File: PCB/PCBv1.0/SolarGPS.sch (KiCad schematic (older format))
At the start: 53 parts, among them J1 Conn_01x10_Female, J2 Solar1+, J3 GND, J4 Conn_02x05_Odd_Even, J5 Solar2+, J6 GND, J7 Screw_Terminal_01x01, U2 MAX-M10Q, U3 MAX40200AUK, U4 STM32WB5MMGH6TR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

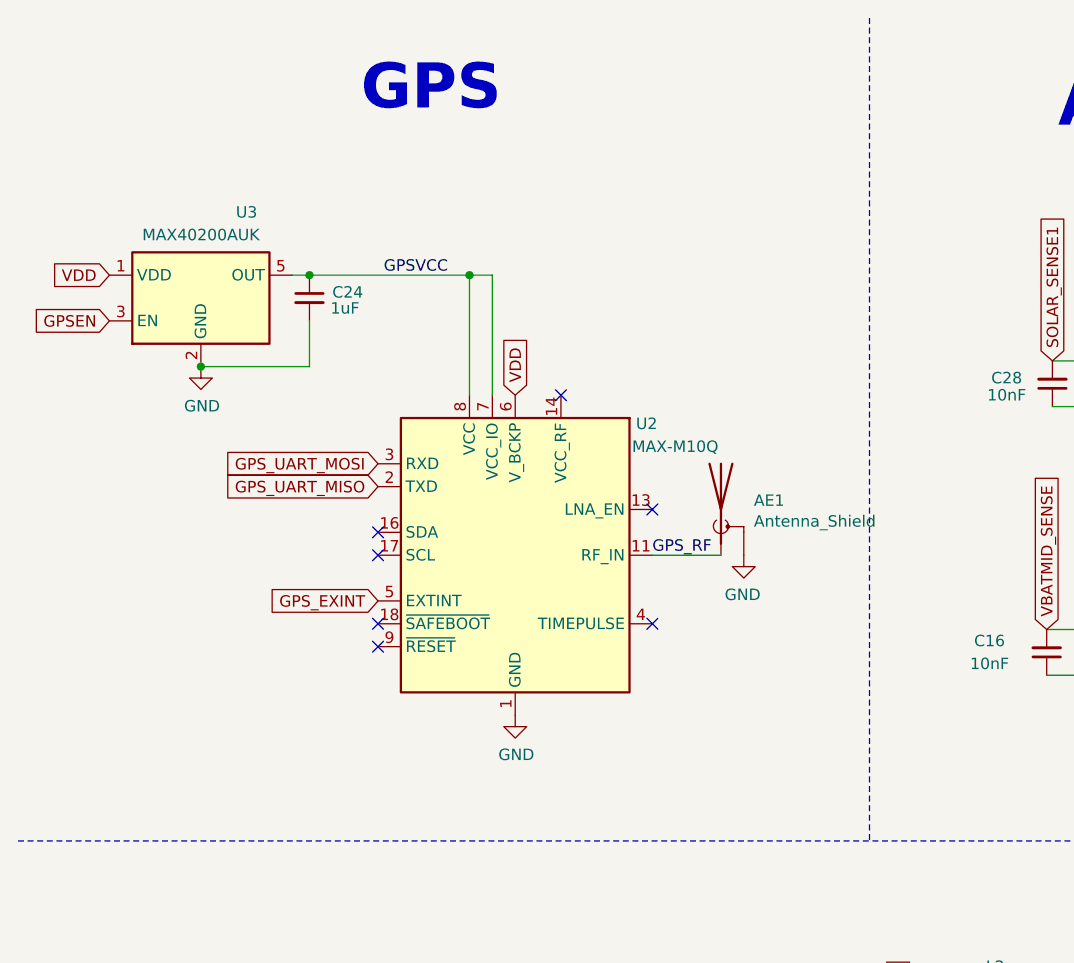
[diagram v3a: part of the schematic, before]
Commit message: Replace Antenna
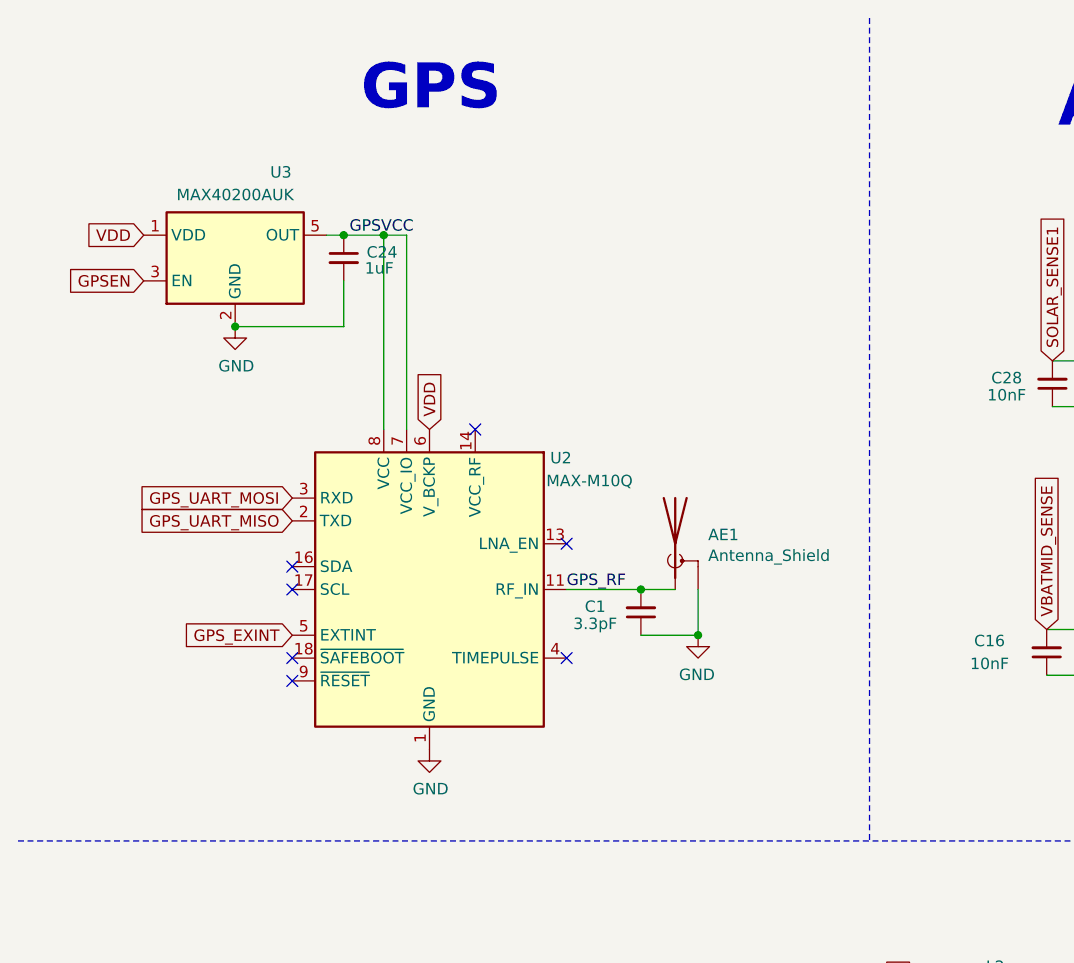
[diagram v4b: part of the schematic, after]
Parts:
- added C1: 3.3pF, Capacitor_SMD:C_0402_1005Metric, symbol Device:C_Small
- AE1: footprint Margo_Lib:LINX_CONSMA002-SMD -> RF_Antenna:Pulse_W3011; Part (none) -> W3011A
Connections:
- net GND: now also C1.1
- net GPS_RF: now also C1.2
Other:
- moved on the sheet: AE1, C24, U2, U3
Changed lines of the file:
@@
 Text GLabel 5000 1975 1    50   Input ~ 0
 SOLAR_SENSE1
-Connection ~ 1750 1600
+Connection ~ 1900 1425
 $Comp
 L Device:C_Small C24
 U 1 1 5FA4FE7E
-P 1750 1700
-F 0 "C24" H 1850 1725 50  0000 L CNN
-F 1 "1uF" H 1842 1655 50  0000 L CNN
-F 2 "Capacitor_SMD:C_0603_1608Metric" H 1750 1700 50  0001 C CNN
-F 3 "~" H 1750 1700 50  0001 C CNN
-	1    1750 1700
-	1    0    0    -1
-$EndComp
-Text GLabel 2050 3025 0    50   Input ~ 0
+P 1900 1525
+F 0 "C24" H 2000 1550 50  0000 L CNN
+F 1 "1uF" H 1992 1480 50  0000 L CNN
+F 2 "Capacitor_SMD:C_0603_1608Metric" H 1900 1525 50  0001 C CNN
+F 3 "~" H 1900 1525 50  0001 C CNN
+	1    1900 1525
+	1    0    0    -1
+$EndComp
+Text GLabel 1675 3175 0    50   Input ~ 0
 GPS_EXINT
 $Comp
 L power:GND #PWR015
 U 1 1 5FA4E6CF
-P 2650 3525
-F 0 "#PWR015" H 2650 3275 50  0001 C CNN
-F 1 "GND" H 2655 3352 50  0000 C CNN
-F 2 "" H 2650 3525 50  0001 C CNN
-F 3 "" H 2650 3525 50  0001 C CNN
-	1    2650 3525
+P 2275 3675
+F 0 "#PWR015" H 2275 3425 50  0001 C CNN
+F 1 "GND" H 2280 3502 50  0000 C CNN
+F 2 "" H 2275 3675 50  0001 C CNN
+F 3 "" H 2275 3675 50  0001 C CNN
+	1    2275 3675
 	1    0    0    -1
 $EndComp
@@
 L RF_GPS:MAX-M8Q U2
 U 1 1 6017075D
-P 2650 2825
-F 0 "U2" H 3225 3400 50  0000 C CNN
-F 1 "MAX-M10Q" H 3350 3300 50  0000 C CNN
-F 2 "RF_GPS:ublox_MAX" H 3050 2175 50  0001 C CNN
-F 3 "https://www.u-blox.com/sites/default/files/MAX-M8-FW3_DataSheet_%28UBX-15031506%29.pdf" H 2650 2825 50  0001 C CNN
-	1    2650 2825
-	1    0    0    -1
-$EndComp
-NoConn ~ 2050 2725
-NoConn ~ 2050 2825
-NoConn ~ 2050 3125
-NoConn ~ 2050 3225
-NoConn ~ 3250 3125
-NoConn ~ 3250 2625
-NoConn ~ 2850 2125
-Text GLabel 2050 2425 0    50   Input ~ 0
+P 2275 2975
+F 0 "U2" H 2850 3550 50  0000 C CNN
+F 1 "MAX-M10Q" H 2975 3450 50  0000 C CNN
+F 2 "RF_GPS:ublox_MAX" H 2675 2325 50  0001 C CNN
+F 3 "https://www.u-blox.com/sites/default/files/MAX-M8-FW3_DataSheet_%28UBX-15031506%29.pdf" H 2275 2975 50  0001 C CNN
+	1    2275 2975
+	1    0    0    -1
+$EndComp
+NoConn ~ 1675 2875
+NoConn ~ 1675 2975
+NoConn ~ 1675 3275
+NoConn ~ 1675 3375
+NoConn ~ 2875 3275
+NoConn ~ 2875 2775
+NoConn ~ 2475 2275
+Text GLabel 1675 2575 0    50   Input ~ 0
 GPS_UART_MOSI
-Text GLabel 2050 2525 0    50   Input ~ 0
+Text GLabel 1675 2675 0    50   Input ~ 0
 GPS_UART_MISO
 Wire Wire Line
@@
 Wire Wire Line
 	4425 7550 4425 7050
-Text GLabel 875  1600 0    50   Input ~ 0
+Text GLabel 1025 1425 0    50   Input ~ 0
 VDD
 Wire Wire Line
-	1675 1600 1750 1600
+	1825 1425 1900 1425
 $Comp
 L Connector:Conn_01x10_Female J1
@@
 SPI_MOSI
 Wire Wire Line
-	3250 2825 3550 2825
+	2875 2975 3200 2975
 Wire Wire Line
 	5675 3150 5950 3150
@@
 L Analog_Switch:MAX40200AUK U3
 U 1 1 61BA8BAE
-P 1275 1700
-F 0 "U3" H 1475 2075 50  0000 C CNN
-F 1 "MAX40200AUK" H 1275 1976 50  0000 C CNN
-F 2 "Package_TO_SOT_SMD:SOT-23-5" H 1275 2200 50  0001 C CNN
-F 3 "https://datasheets.maximintegrated.com/en/ds/MAX40200.pdf" H 1275 2200 50  0001 C CNN
-	1    1275 1700
-	1    0    0    -1
-$EndComp
-Text GLabel 875  1800 0    50   Input ~ 0
+P 1425 1525
+F 0 "U3" H 1625 1900 50  0000 C CNN
+F 1 "MAX40200AUK" H 1425 1801 50  0000 C CNN
+F 2 "Package_TO_SOT_SMD:SOT-23-5" H 1425 2025 50  0001 C CNN
+F 3 "https://datasheets.maximintegrated.com/en/ds/MAX40200.pdf" H 1425 2025 50  0001 C CNN
+	1    1425 1525
+	1    0    0    -1
+$EndComp
+Text GLabel 1025 1625 0    50   Input ~ 0
 GPSEN
 $Comp
 L power:GND #PWR06
 U 1 1 61BB7ABB
-P 1275 2000
-F 0 "#PWR06" H 1275 1750 50  0001 C CNN
-F 1 "GND" H 1280 1827 50  0000 C CNN
-F 2 "" H 1275 2000 50  0001 C CNN
-F 3 "" H 1275 2000 50  0001 C CNN
-	1    1275 2000
+P 1425 1825
+F 0 "#PWR06" H 1425 1575 50  0001 C CNN
+F 1 "GND" H 1430 1652 50  0000 C CNN
+F 2 "" H 1425 1825 50  0001 C CNN
+F 3 "" H 1425 1825 50  0001 C CNN
+	1    1425 1825
 	1    0    0    -1
 $EndComp
@@
 	0    1    -1   0
 $EndComp
-Text Label 3250 2825 0    50   ~ 0
+Text Label 2875 2975 0    50   ~ 0
 GPS_RF
 $Comp
 L Device:Antenna_Shield AE1
 U 1 1 61D38EF7
-P 3550 2625
-F 0 "AE1" H 3694 2664 50  0000 L CNN
-F 1 "Antenna_Shield" H 3694 2573 50  0000 L CNN
-F 2 "Margo_Lib:LINX_CONSMA002-SMD" H 3550 2725 50  0001 C CNN
-F 3 "~" H 3550 2725 50  0001 C CNN
-	1    3550 2625
+P 3350 2775
+F 0 "AE1" H 3494 2814 50  0000 L CNN
+F 1 "Antenna_Shield" H 3494 2723 50  0000 L CNN
+F 2 "RF_Antenna:Pulse_W3011" H 3350 2875 50  0001 C CNN
+F 3 "~" H 3350 2875 50  0001 C CNN
+F 4 "W3011A" H 3350 2775 50  0001 C CNN "Part"
+	1    3350 2775
 	1    0    0    -1
 $EndComp
@@
 L power:GND #PWR0101
 U 1 1 61D3AA3F
-P 3650 2825
-F 0 "#PWR0101" H 3650 2575 50  0001 C CNN
-F 1 "GND" H 3655 2652 50  0000 C CNN
-F 2 "" H 3650 2825 50  0001 C CNN
-F 3 "" H 3650 2825 50  0001 C CNN
-	1    3650 2825
+P 3450 3175
+F 0 "#PWR0101" H 3450 2925 50  0001 C CNN
+F 1 "GND" H 3455 3002 50  0000 C CNN
+F 2 "" H 3450 3175 50  0001 C CNN
+F 3 "" H 3450 3175 50  0001 C CNN
+	1    3450 3175
 	-1   0    0    -1
 $EndComp
@@
 Text GLabel 8000 5375 1    50   Input ~ 0
 VDD
-Text Label 2075 1600 0    50   ~ 0
+Text Label 1925 1425 0    50   ~ 0
 GPSVCC
 Text GLabel 7400 5375 1    50   Input ~ 0
@@
 Connection ~ 5200 5575
 Wire Wire Line
-	2450 2125 2450 1600
-Connection ~ 2450 1600
-Wire Wire Line
-	2450 1600 2550 1600
-Wire Wire Line
-	2550 2125 2550 1600
-Text GLabel 2650 2125 1    50   Input ~ 0
+	2075 2275 2075 1425
+Wire Wire Line
+	2075 1425 2175 1425
+Wire Wire Line
+	2175 2275 2175 1425
+Text GLabel 2275 2275 1    50   Input ~ 0
 VDD
 Wire Wire Line
-	1275 2000 1750 2000
-Wire Wire Line
-	1750 2000 1750 1800
-Connection ~ 1275 2000
+	1425 1825 1900 1825
+Wire Wire Line
+	1900 1825 1900 1625
+Connection ~ 1425 1825
 Text GLabel 12350 975  2    50   Input ~ 0
 VDD
@@
 $EndComp
 Wire Wire Line
-	1750 1600 2450 1600
+	1900 1425 2075 1425
 $Comp
 L Device:C_Small C25
@@
 Text Label 1350 6050 1    50   ~ 0
 SOLAR+
+$Comp
+L Device:C_Small C1
+U 1 1 61AA34D0
+P 3200 3075
+F 0 "C1" H 3000 3050 50  0000 C CNN
+F 1 "3.3pF" H 3000 3125 50  0000 C CNN
+F 2 "Capacitor_SMD:C_0402_1005Metric" H 3200 3075 50  0001 C CNN
+F 3 "~" H 3200 3075 50  0001 C CNN
+	1    3200 3075
+	1    0    0    1
+$EndComp
+Connection ~ 2075 1425
+Connection ~ 3200 2975
+Wire Wire Line
+	3200 2975 3350 2975
+Wire Wire Line
+	3200 3175 3450 3175
+Wire Wire Line
+	3450 3175 3450 2975
+Connection ~ 3450 3175
 $EndSCHEMATC

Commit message: Redraw PCB1.0
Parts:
- added C10, C11, C13: 3.3pF, Capacitor_SMD:C_0402_1005Metric, symbol Device:C_Small
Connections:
- net GND: now also U4.42 (PE4), C10.1, C11.1, C13.1; no longer U4.75 (PD8)
- net GPS_UART_MISO: now also C11.2
- net GPS_UART_MOSI: now also C13.2
- net LED: now also C10.2
- net SOLAR_SENSE2: no longer names the net of U4.56 (PA3)
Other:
- moved on the sheet: C26, D2, R3
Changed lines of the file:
@@
 L Device:LED D2
 U 1 1 61AE613D
-P 9675 3725
-F 0 "D2" V 9700 3850 50  0000 C CNN
-F 1 "LED" V 9625 3875 50  0000 C CNN
-F 2 "Diode_SMD:D_0805_2012Metric" H 9675 3725 50  0001 C CNN
-F 3 "~" H 9675 3725 50  0001 C CNN
-F 4 "LS R976-NR-1" H 9675 3725 50  0001 C CNN "Part"
-	1    9675 3725
+P 9575 3725
+F 0 "D2" V 9600 3850 50  0000 C CNN
+F 1 "LED" V 9525 3875 50  0000 C CNN
+F 2 "Diode_SMD:D_0805_2012Metric" H 9575 3725 50  0001 C CNN
+F 3 "~" H 9575 3725 50  0001 C CNN
+F 4 "LS R976-NR-1" H 9575 3725 50  0001 C CNN "Part"
+	1    9575 3725
 	0    1    -1   0
 $EndComp
@@
 F 3 "" H 12350 4075 50  0001 C CNN
 	1    12350 4075
-	0    -1   -1   0
-$EndComp
-$Comp
-L power:GND #PWR0114
-U 1 1 61BC97E0
-P 12350 3975
-F 0 "#PWR0114" H 12350 3725 50  0001 C CNN
-F 1 "GND" H 12355 3802 50  0000 C CNN
-F 2 "" H 12350 3975 50  0001 C CNN
-F 3 "" H 12350 3975 50  0001 C CNN
-	1    12350 3975
 	0    -1   -1   0
 $EndComp
@@
 	1    0    0    -1
 $EndComp
-Text GLabel 10750 2875 0    50   Input ~ 0
-SOLAR_SENSE2
 Text GLabel 12350 2675 2    50   Input ~ 0
 GPSEN
@@
 Text GLabel 10750 4475 0    50   Input ~ 0
 LED
-Text GLabel 9675 3375 1    50   Input ~ 0
+Text GLabel 9575 3375 1    50   Input ~ 0
 LED
 $Comp
 L Device:R_Small R3
 U 1 1 61AF4E77
-P 9675 3475
-F 0 "R3" H 9550 3500 50  0000 C CNN
-F 1 "390" H 9550 3425 50  0000 C CNN
-F 2 "Resistor_SMD:R_0603_1608Metric" H 9675 3475 50  0001 C CNN
-F 3 "~" H 9675 3475 50  0001 C CNN
-	1    9675 3475
+P 9575 3475
+F 0 "R3" H 9450 3500 50  0000 C CNN
+F 1 "390" H 9450 3425 50  0000 C CNN
+F 2 "Resistor_SMD:R_0603_1608Metric" H 9575 3475 50  0001 C CNN
+F 3 "~" H 9575 3475 50  0001 C CNN
+	1    9575 3475
 	-1   0    0    -1
 $EndComp
 Wire Wire Line
-	9675 3950 9675 3875
+	9575 3950 9575 3875
 $Comp
 L power:GND #PWR0102
 U 1 1 61AED265
-P 9675 3950
-F 0 "#PWR0102" H 9675 3700 50  0001 C CNN
-F 1 "GND" H 9680 3777 50  0000 C CNN
-F 2 "" H 9675 3950 50  0001 C CNN
-F 3 "" H 9675 3950 50  0001 C CNN
-	1    9675 3950
+P 9575 3950
+F 0 "#PWR0102" H 9575 3700 50  0001 C CNN
+F 1 "GND" H 9580 3777 50  0000 C CNN
+F 2 "" H 9575 3950 50  0001 C CNN
+F 3 "" H 9575 3950 50  0001 C CNN
+	1    9575 3950
 	-1   0    0    -1
 $EndComp
@@
 L Device:C_Small C26
 U 1 1 61A8ADD1
-P 8650 2400
-F 0 "C26" H 8742 2446 50  0000 L CNN
-F 1 "1uF" H 8742 2355 50  0000 L CNN
-F 2 "Capacitor_SMD:C_0603_1608Metric" H 8650 2400 50  0001 C CNN
-F 3 "~" H 8650 2400 50  0001 C CNN
-	1    8650 2400
+P 8750 2750
+F 0 "C26" H 8842 2796 50  0000 L CNN
+F 1 "1uF" H 8842 2705 50  0000 L CNN
+F 2 "Capacitor_SMD:C_0603_1608Metric" H 8750 2750 50  0001 C CNN
+F 3 "~" H 8750 2750 50  0001 C CNN
+	1    8750 2750
 	1    0    0    1
 $EndComp
@@
 	1    0    0    -1
 $EndComp
-Text GLabel 8650 2300 1    50   Input ~ 0
+Text GLabel 8750 2650 1    50   Input ~ 0
 VDD
 $Comp
 L power:GND #PWR0127
 U 1 1 61A8B666
-P 8650 2500
-F 0 "#PWR0127" H 8650 2250 50  0001 C CNN
-F 1 "GND" H 8655 2327 50  0000 C CNN
-F 2 "" H 8650 2500 50  0001 C CNN
-F 3 "" H 8650 2500 50  0001 C CNN
-	1    8650 2500
+P 8750 2850
+F 0 "#PWR0127" H 8750 2600 50  0001 C CNN
+F 1 "GND" H 8755 2677 50  0000 C CNN
+F 2 "" H 8750 2850 50  0001 C CNN
+F 3 "" H 8750 2850 50  0001 C CNN
+	1    8750 2850
 	1    0    0    -1
 $EndComp
@@
 	3450 3175 3450 2975
 Connection ~ 3450 3175
+$Comp
+L Device:C_Small C13
+U 1 1 61C04415
+P 13175 3800
+F 0 "C13" H 12975 3775 50  0000 C CNN
+F 1 "3.3pF" H 12975 3850 50  0000 C CNN
+F 2 "Capacitor_SMD:C_0402_1005Metric" H 13175 3800 50  0001 C CNN
+F 3 "~" H 13175 3800 50  0001 C CNN
+	1    13175 3800
+	-1   0    0    1
+$EndComp
+Text GLabel 13175 3700 1    50   Input ~ 0
+GPS_UART_MOSI
+Text GLabel 13025 3700 1    50   Input ~ 0
+GPS_UART_MISO
+$Comp
+L Device:C_Small C11
+U 1 1 61C084B0
+P 13025 3800
+F 0 "C11" H 13375 3700 50  0000 C CNN
+F 1 "3.3pF" H 13375 3850 50  0000 C CNN
+F 2 "Capacitor_SMD:C_0402_1005Metric" H 13025 3800 50  0001 C CNN
+F 3 "~" H 13025 3800 50  0001 C CNN
+	1    13025 3800
+	1    0    0    1
+$EndComp
+$Comp
+L power:GND #PWR03
+U 1 1 61C086CE
+P 13025 3900
+F 0 "#PWR03" H 13025 3650 50  0001 C CNN
+F 1 "GND" H 13030 3727 50  0000 C CNN
+F 2 "" H 13025 3900 50  0001 C CNN
+F 3 "" H 13025 3900 50  0001 C CNN
+	1    13025 3900
+	1    0    0    -1
+$EndComp
+Text GLabel 12875 3700 1    50   Input ~ 0
+LED
+$Comp
+L Device:C_Small C10
+U 1 1 61C1A1DF
+P 12875 3800
+F 0 "C10" H 13375 3625 50  0000 C CNN
+F 1 "3.3pF" H 13375 3850 50  0000 C CNN
+F 2 "Capacitor_SMD:C_0402_1005Metric" H 12875 3800 50  0001 C CNN
+F 3 "~" H 12875 3800 50  0001 C CNN
+	1    12875 3800
+	1    0    0    1
+$EndComp
+Wire Wire Line
+	12875 3900 13025 3900
+Connection ~ 13175 3900
+Connection ~ 13025 3900
+Wire Wire Line
+	13025 3900 13175 3900
+$Comp
+L power:GND #PWR?
+U 1 1 61C4C8E4
+P 12350 5275
+F 0 "#PWR?" H 12350 5025 50  0001 C CNN
+F 1 "GND" H 12355 5102 50  0000 C CNN
+F 2 "" H 12350 5275 50  0001 C CNN
+F 3 "" H 12350 5275 50  0001 C CNN
+	1    12350 5275
+	0    -1   -1   0
+$EndComp
 $EndSCHEMATC
